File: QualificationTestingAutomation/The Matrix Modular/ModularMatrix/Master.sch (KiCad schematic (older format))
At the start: 12 parts, among them J2 Raspberry_Pi_2_3, U7 TC2050-JTAG-SchematicAutomati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

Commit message: Added Voltage and current measurment of the muxes and relays to the MSP Some clean up of the tracks.
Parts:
- removed U7: TC2050-JTAG-SchematicAutomation-rescue, symbol TheMatrix-rescue:TC2050-JTAG-SchematicAutomation-rescue
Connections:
- wire segments 45 -> 41
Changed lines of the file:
@@
 	1    0    0    -1
 $EndComp
-$Comp
-L TheMatrix-rescue:TC2050-JTAG-SchematicAutomation-rescue U7
-U 1 1 5C8E1E87
-P 2650 4000
-F 0 "U7" H 2650 4165 50  0000 C CNN
-F 1 "TC2050-JTAG-SchematicAutomation-rescue" H 2650 4074 50  0000 C CNN
-F 2 "" H 2650 4000 50  0001 C CNN
-F 3 "" H 2650 4000 50  0001 C CNN
-	1    2650 4000
-	1    0    0    -1
-$EndComp
-$Comp
-L power:+3V3 #PWR0103
-U 1 1 5C8E1FB5
-P 1750 4000
-F 0 "#PWR0103" H 1750 3850 50  0001 C CNN
-F 1 "+3V3" H 1765 4173 50  0000 C CNN
-F 2 "" H 1750 4000 50  0001 C CNN
-F 3 "" H 1750 4000 50  0001 C CNN
-	1    1750 4000
-	1    0    0    -1
-$EndComp
-Wire Wire Line
-	2150 4100 1750 4100
-Wire Wire Line
-	1750 4100 1750 4000
-Text GLabel 1900 4200 0    50   Input ~ 0
-TMS
-Text GLabel 1900 4400 0    50   Input ~ 0
-TCK
-Text GLabel 3150 4100 2    50   Input ~ 0
-TDO
-Text GLabel 3150 4300 2    50   Input ~ 0
-TDI
-Wire Wire Line
-	2150 4200 1900 4200
-Wire Wire Line
-	2150 4400 1900 4400
 Text GLabel 1500 4900 2    50   Input ~ 0
 TDO

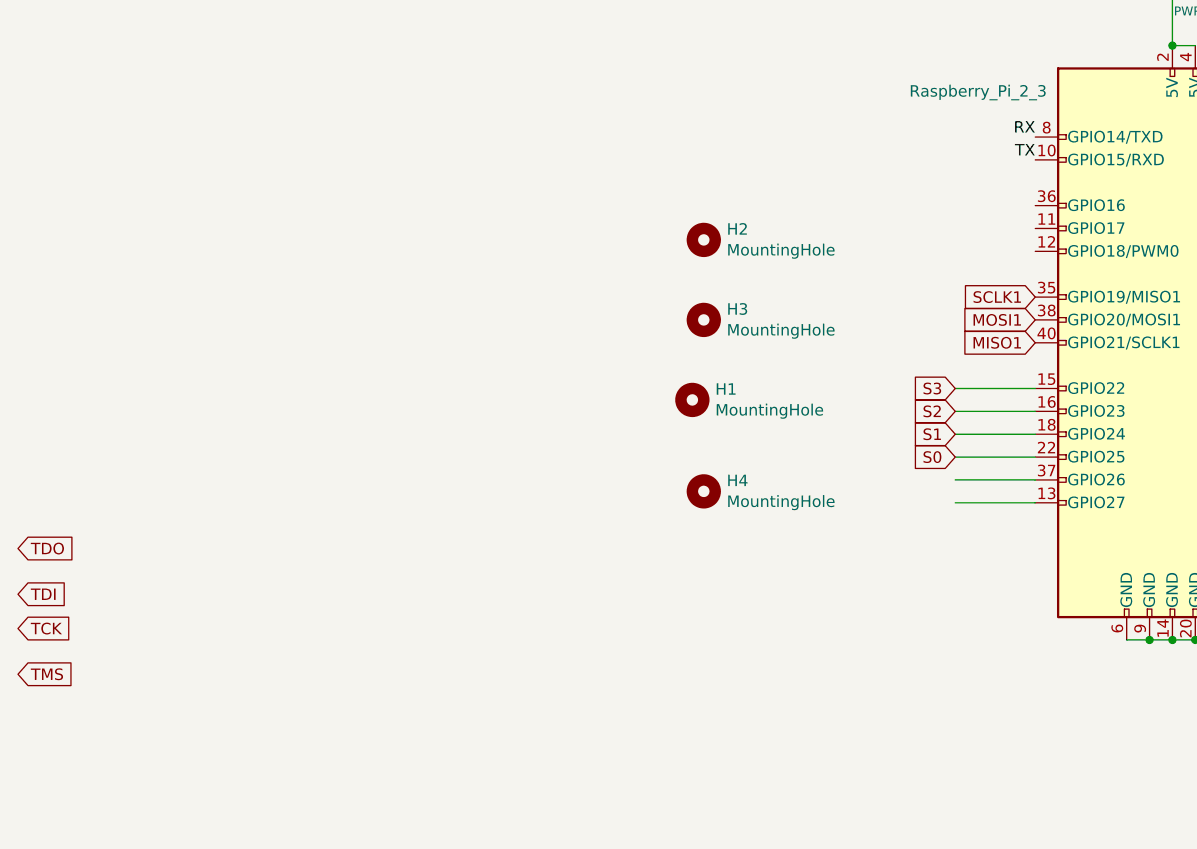
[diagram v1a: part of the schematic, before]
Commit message: Schematic Clean ups the layout needs to be changed
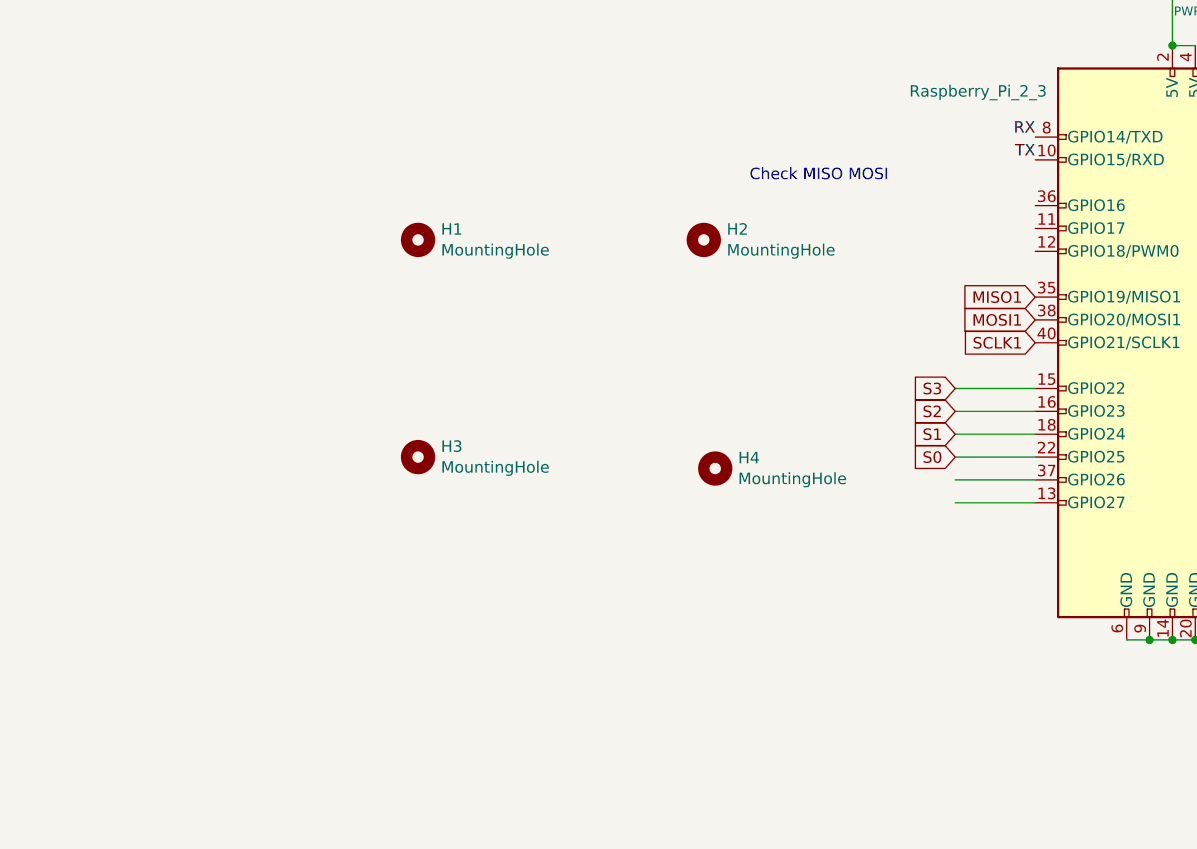
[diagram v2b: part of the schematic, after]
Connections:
- net labels removed: TCK, TDI, TDO, TMS
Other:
- note added: "Check MISO MOSI"
- moved on the sheet: H1, H3, H4
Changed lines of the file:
@@
 EESchema Schematic File Version 4
 LIBS:ModularMatrix-cache
-EELAYER 26 0
+EELAYER 29 0
 EELAYER END
 $Descr A4 11693 8268
@@
 L Mechanical:MountingHole H3
 U 1 1 5E7B1ABE
-P 4500 3900
-F 0 "H3" H 4600 3946 50  0000 L CNN
-F 1 "MountingHole" H 4600 3855 50  0000 L CNN
-F 2 "MountingHole:MountingHole_2.5mm" H 4500 3900 50  0001 C CNN
-F 3 "~" H 4500 3900 50  0001 C CNN
-	1    4500 3900
+P 3250 4500
+F 0 "H3" H 3350 4546 50  0000 L CNN
+F 1 "MountingHole" H 3350 4455 50  0000 L CNN
+F 2 "MountingHole:MountingHole_2.5mm" H 3250 4500 50  0001 C CNN
+F 3 "~" H 3250 4500 50  0001 C CNN
+	1    3250 4500
 	1    0    0    -1
 $EndComp
@@
 L Mechanical:MountingHole H1
 U 1 1 5E7B23E4
-P 4450 4250
-F 0 "H1" H 4550 4296 50  0000 L CNN
-F 1 "MountingHole" H 4550 4205 50  0000 L CNN
-F 2 "MountingHole:MountingHole_2.5mm" H 4450 4250 50  0001 C CNN
-F 3 "~" H 4450 4250 50  0001 C CNN
-	1    4450 4250
+P 3250 3550
+F 0 "H1" H 3350 3596 50  0000 L CNN
+F 1 "MountingHole" H 3350 3505 50  0000 L CNN
+F 2 "MountingHole:MountingHole_2.5mm" H 3250 3550 50  0001 C CNN
+F 3 "~" H 3250 3550 50  0001 C CNN
+	1    3250 3550
 	1    0    0    -1
 $EndComp
@@
 L Mechanical:MountingHole H4
 U 1 1 5E7B2D0B
-P 4500 4650
-F 0 "H4" H 4600 4696 50  0000 L CNN
-F 1 "MountingHole" H 4600 4605 50  0000 L CNN
-F 2 "MountingHole:MountingHole_2.5mm" H 4500 4650 50  0001 C CNN
-F 3 "~" H 4500 4650 50  0001 C CNN
-	1    4500 4650
-	1    0    0    -1
-$EndComp
-Text GLabel 1500 4900 2    50   Input ~ 0
-TDO
-Text GLabel 1500 5100 2    50   Input ~ 0
-TDI
-Text GLabel 1500 5450 2    50   Input ~ 0
-TMS
-Text GLabel 1500 5250 2    50   Input ~ 0
-TCK
+P 4550 4550
+F 0 "H4" H 4650 4596 50  0000 L CNN
+F 1 "MountingHole" H 4650 4505 50  0000 L CNN
+F 2 "MountingHole:MountingHole_2.5mm" H 4550 4550 50  0001 C CNN
+F 3 "~" H 4550 4550 50  0001 C CNN
+	1    4550 4550
+	1    0    0    -1
+$EndComp
 Text GLabel 5950 3900 0    50   Input ~ 0
 MOSI1
+Text GLabel 5950 4000 0    50   Input ~ 0
+SCLK1
 Text GLabel 5950 3800 0    50   Input ~ 0
-SCLK1
-Text GLabel 5950 4000 0    50   Input ~ 0
 MISO1
+Text Notes 4700 3300 0    50   ~ 0
+Check MISO MOSI
 $EndSCHEMATC

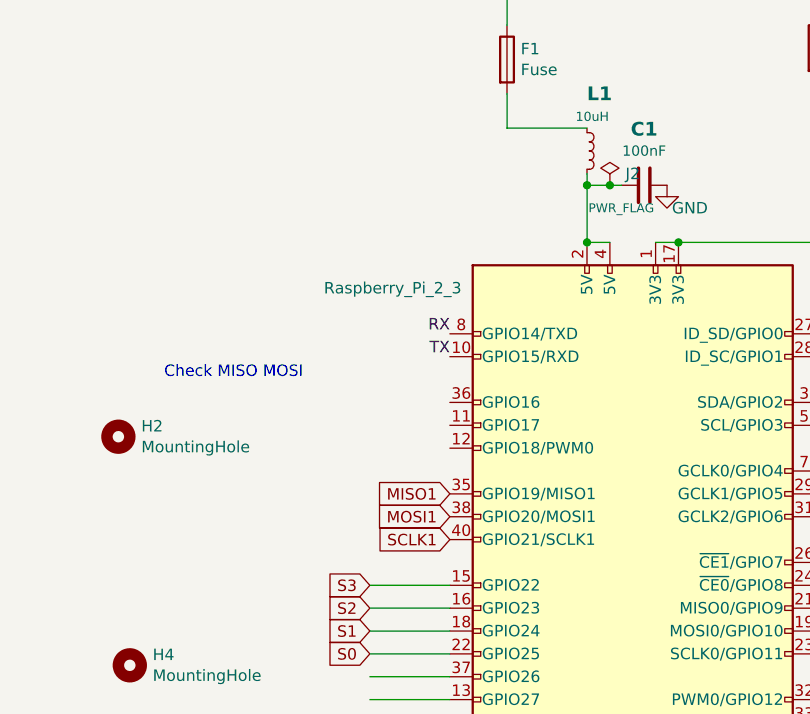
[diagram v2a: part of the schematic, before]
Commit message: IO clean up added the 1v25 reference to Matrix Changed Some of the labels to more legible names.
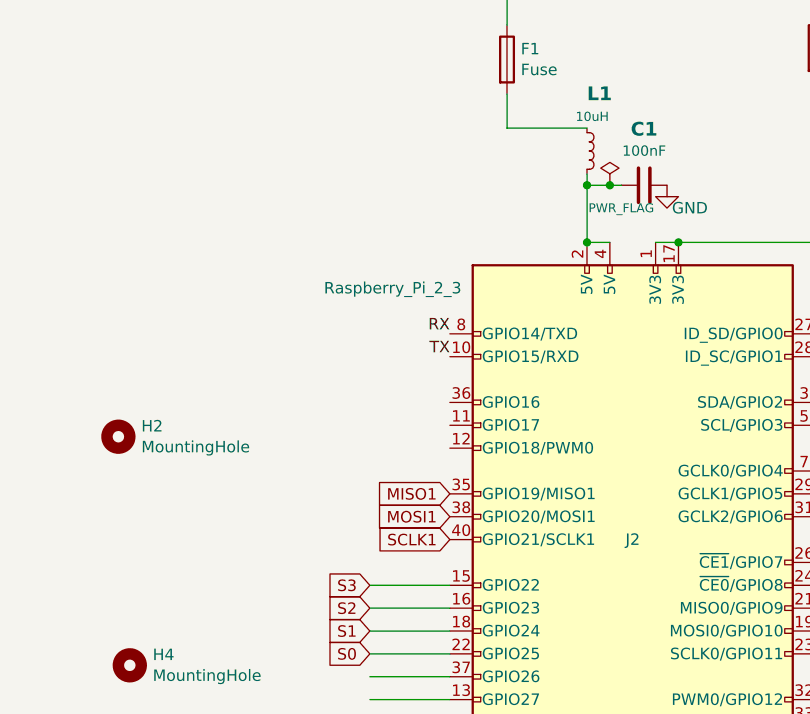
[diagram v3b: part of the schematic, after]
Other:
- note removed: "Check MISO MOSI"
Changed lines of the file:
@@
 U 1 1 5C876E55
 P 6750 4000
-F 0 "J2" H 6750 5600 50  0000 C CNN
+F 0 "J2" H 6750 4000 50  0000 C CNN
 F 1 "Raspberry_Pi_2_3" H 5700 5100 50  0000 C CNN
 F 2 "Connector_PinSocket_2.54mm:PinSocket_2x20_P2.54mm_Vertical_SMD" H 6750 4000 50  0001 C CNN
@@
 Text GLabel 5950 3800 0    50   Input ~ 0
 MISO1
-Text Notes 4700 3300 0    50   ~ 0
-Check MISO MOSI
 $EndSCHEMATC
